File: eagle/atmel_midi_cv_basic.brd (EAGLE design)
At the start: 100 x 80.8 mm, 46 parts, among them IC1 TL072P, IC2 TL072P, U1 ATMEGA328P_PDIP

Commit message: fixed led output to pwm pin and schematic consistent
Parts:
- R25: value 220 -> 470
- moved VEL_LED 39.1 mm to (28.7, 10.2), turned to 270 degrees
- moved R25 22.5 mm to (32.0, 19.1)
- moved C6 17.5 mm to (24.6, 6.35)
- moved R12 14.2 mm to (29.1, 20.6)
- moved C2 13.7 mm to (25.7, 26.4)
- moved R13 13.3 mm to (21.6, 25.4)
- moved C5 12.2 mm to (58.9, 53.3)
- moved CV_BUS_ENABLE 12.2 mm to (69.7, 51.6)
- moved PITCH 12.2 mm to (72.9, 0.00)
- moved R10 12.2 mm to (72.1, 43.2)
- moved R11 12.2 mm to (62.7, 21.6)
- moved R5 12.2 mm to (58.9, 37.8)
- moved R8 12.2 mm to (60.8, 24.8)
- moved SCALE_TRIM 12.2 mm to (62.7, 44.5)
- moved U$4 12.2 mm to (53.8, 25.4)
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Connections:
- new net GND: VEL_LED.K
- net N$18: now also R25.1, VEL_LED.A; no longer R25.2, VEL_LED.K
- net N$20: now also R25.2, U1.12; no longer U1.6, VEL_LED.A
- net N$22: now also U1.6; no longer U1.5
- net N$29: no longer R25.1
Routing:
- net GND: track 0.00 -> 3.72 mm
- net N$28: track 39.6 -> 41.7 mm
- net N$20: track 8.09 -> 6.01 mm
- net +12V: track 144.9 -> 142.9 mm
- net +5V: track 176.7 -> 178.1 mm
- net N$21: track 7.28 -> 8.37 mm
- net N$10: track 13.6 -> 12.9 mm
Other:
- board size 100 x 80.8 mm -> 101 x 80.8 mm

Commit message: cleaned up some routes
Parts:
- R1, R10, R11, R12, R13, R2, R24, R25, R26, R3, R4, R5, R7, R8, R9: device rcl:0207/10 -> rcl:0207/7
- moved R1 3.78 mm to (36.3, 61.0)
- moved R8 3.66 mm to (58.8, 21.7), turned to 90 degrees
- moved RST1 3.21 mm to (29.2, 60.7)
- moved RST2 3.14 mm to (29.2, 64.3)
- moved D1 2.84 mm to (13.2, 52.1)
- moved U$2 2.03 mm to (61.5, 52.1)
- moved VEL_LED 1.83 mm to (29.7, 11.7)
- moved GATE_BUS_ENABLE 1.80 mm to (70.5, 56.3)
- moved R2 1.80 mm to (13.2, 49.5)
- moved CV_BUS_ENABLE 1.78 mm to (67.9, 51.6)
- moved C4 1.48 mm to (53.8, 52.6)
- moved C5 1.37 mm to (57.7, 52.8)
- moved MIDI_IN_4 1.27 mm to (23.4, 50.8)
- moved OK1 1.27 mm to (15.7, 59.7)
- moved SCALE_TRIM 1.27 mm to (62.7, 45.7)
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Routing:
- net N$29: track 346.8 -> 339.8 mm
- net N$32: track 0.00 -> 6.35 mm
- net N$13: track 12.7 -> 7.16 mm
- net +12V: track 142.9 -> 137.6 mm
- net N$9: track 42.8 -> 38.7 mm
- net GND: track 3.72 -> 0.00 mm
- net N$17: track 57.9 -> 54.3 mm
- net N$43: track 7.40 -> 10.7 mm
- net N$30: track 37.7 -> 34.5 mm
- net N$28: track 41.7 -> 44.2 mm
- net N$8: track 4.02 -> 6.48 mm
- net N$27: track 5.80 -> 7.46 mm
- net N$14: track 11.1 -> 9.57 mm
- net N$3: track 10.3 -> 11.7 mm
- net N$7: track 8.90 -> 10.3 mm
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
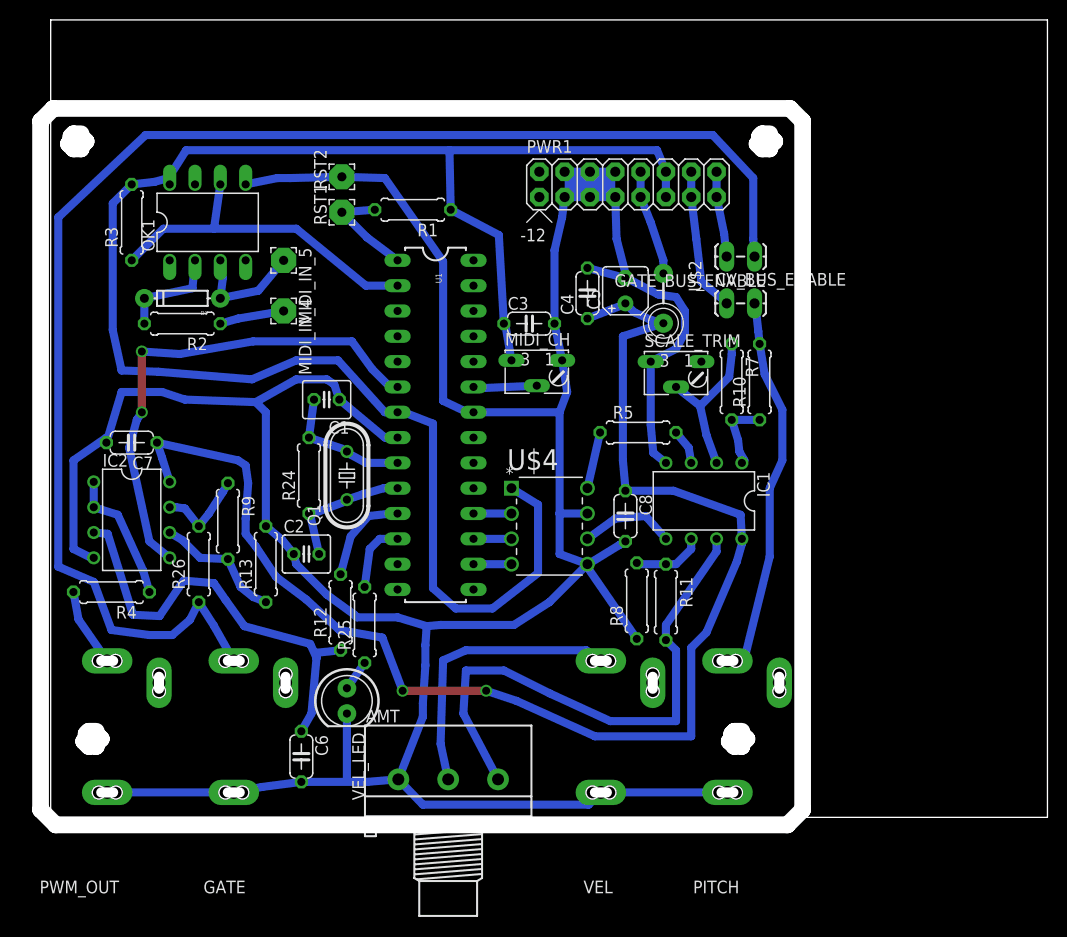
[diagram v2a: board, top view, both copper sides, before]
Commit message: corrected wrong gate pin and tl072 back to bipolar to prevent locking
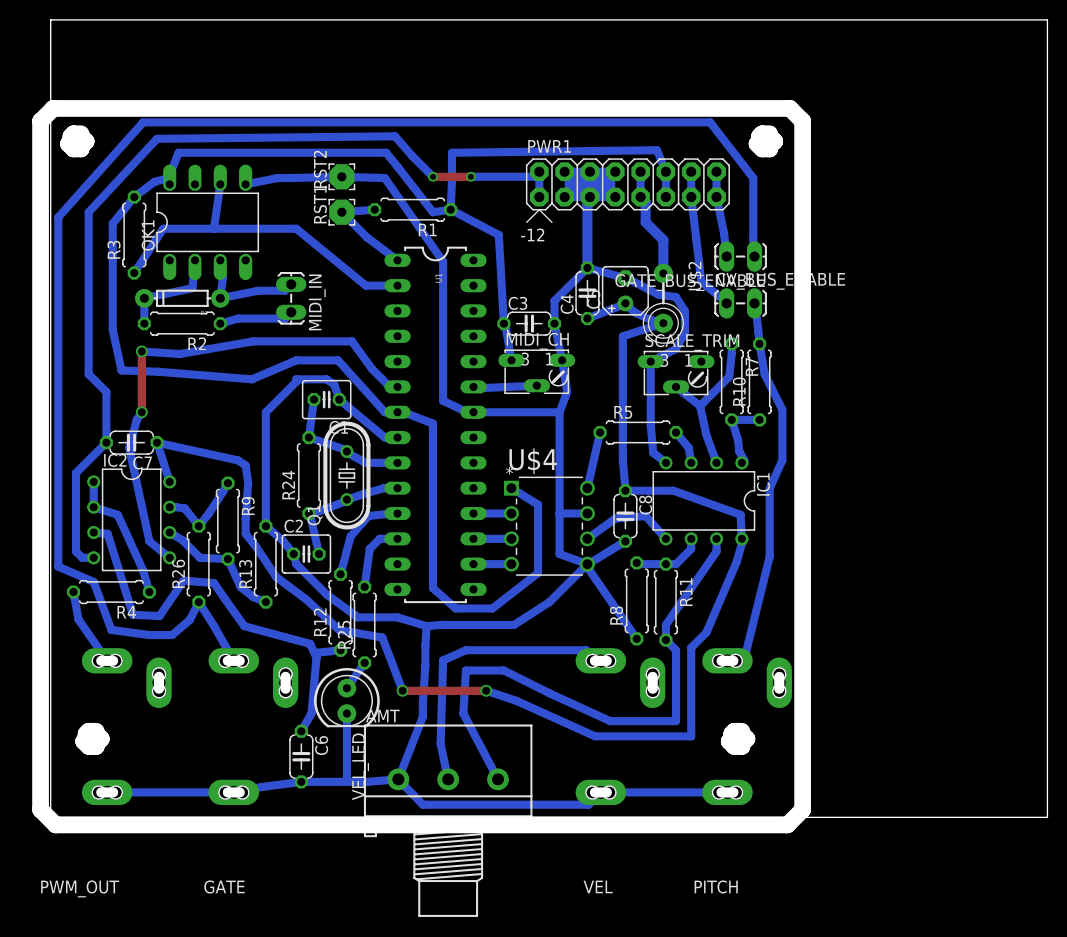
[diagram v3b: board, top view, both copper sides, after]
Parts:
- removed MIDI_IN_4: midi pin 4, wirepad:2,54/0,9
- removed MIDI_IN_5: midi pin 5, wirepad:2,54/0,9
- added MIDI_IN: M02LOCK_LONGPADS, SparkFun-Connectors:1X02_LOCK_LONGPADS
- moved R3 1.30 mm to (8.38, 58.4)
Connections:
- new net -12V: C7.2, IC2.4, PWR1.1, PWR1.2
- net N$29: no longer C7.2, IC2.4
- net N$3: now also MIDI_IN.1; no longer MIDI_IN_5.1
- net N$8: now also MIDI_IN.2; no longer MIDI_IN_4.1
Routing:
- net -12V: track 0.00 -> 91.0 mm, vias 0 -> 2
- net N$29: track 339.8 -> 296.5 mm
- net N$31: track 144.1 -> 146.0 mm
- net +5V: track 176.8 -> 178.5 mm
- net N$8: track 6.48 -> 7.45 mm
- net N$30: track 34.5 -> 35.3 mm
- net N$11: track 10.6 -> 11.1 mm

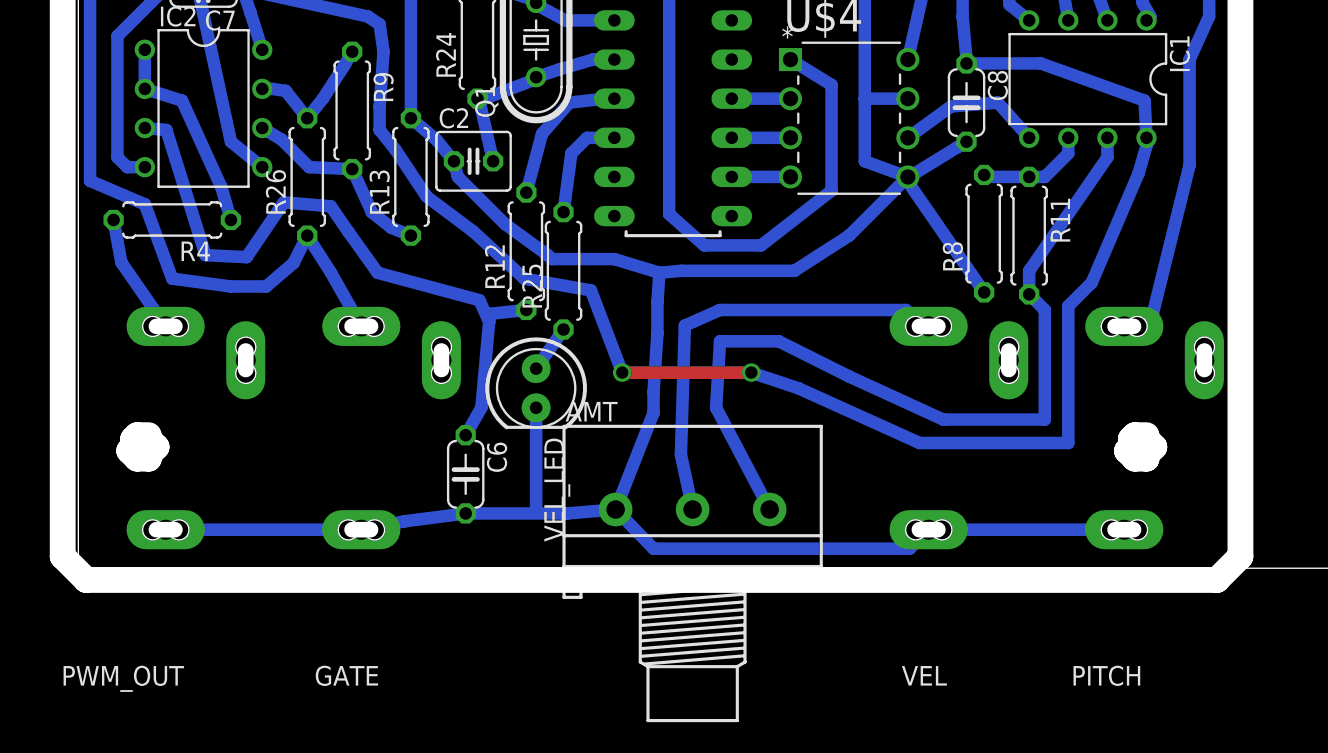
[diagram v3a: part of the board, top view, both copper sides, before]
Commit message: rail2rail pitch amp, tone output, improved decoupling, board mount midi jack, more isolation
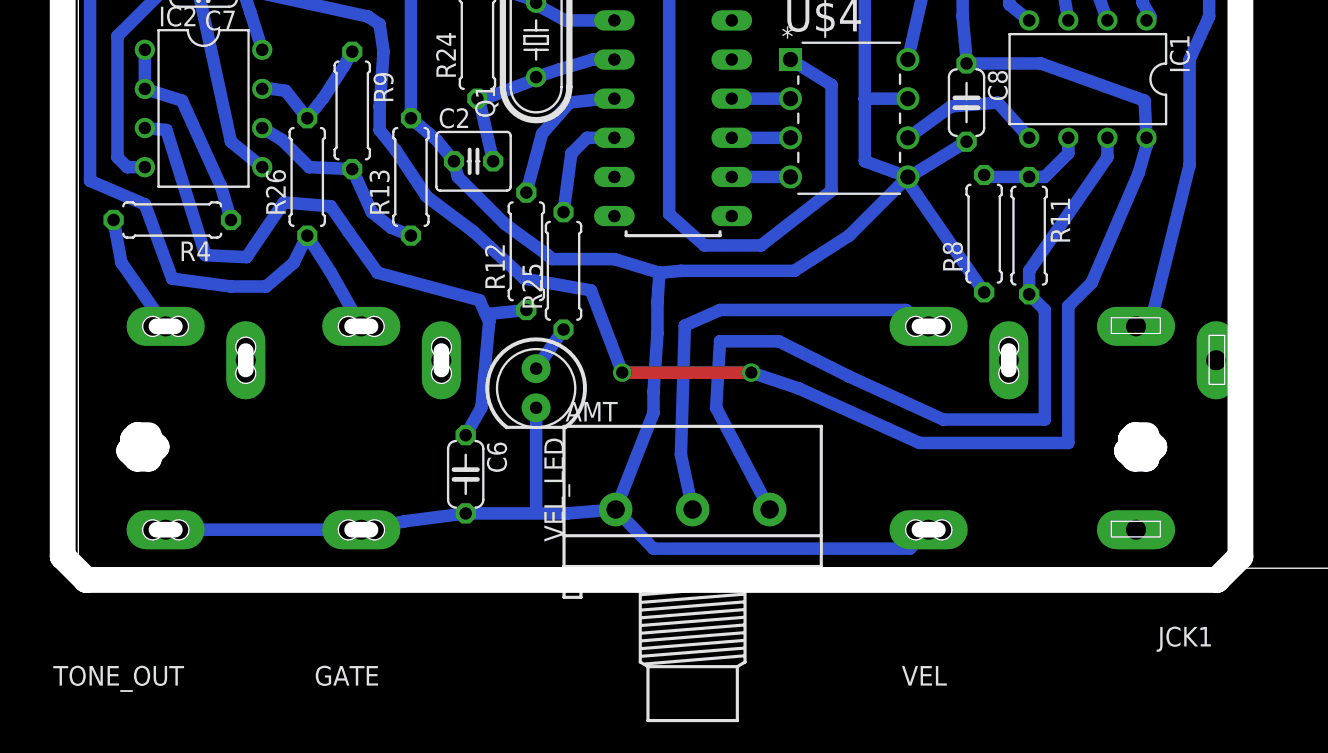
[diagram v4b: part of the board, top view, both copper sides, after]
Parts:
- removed PITCH: AUDIO-JACK, erthenvar:ERTHENVAR-JACK-90DEG
- added JCK1: AUDIO-JACKITEAD, erthenvar:JACK-90DEG-ITEAD
- renumbered PWM_OUT to TONE_OUT
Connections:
- net N$21: now also U1.19; no longer U1.11
- net N$29: now also JCK1.P$1; no longer PITCH.P$1
- net N$9: now also JCK1.P$3; no longer PITCH.P$3
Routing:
- net N$29: track 296.5 -> 283.8 mm
- net N$9: track 38.7 -> 37.1 mm
- net N$21: track 9.58 -> 8.94 mm
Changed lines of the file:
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@@
 <?xml version="1.0" encoding="utf-8"?>
 <!DOCTYPE eagle SYSTEM "eagle.dtd">
-<eagle version="7.1.0">
+<eagle version="7.6.0">
 <drawing>
 <settings>
@@
 <attribute name="OC_FARNELL" value="9860150" x="15.748" y="59.69" size="1.778" layer="27" display="off"/>
 </element>
-<element name="PITCH" library="erthenvar" package="ERTHENVAR-JACK-90DEG" value="AUDIO-JACK" x="72.898" y="0" rot="R180"/>
-<element name="PWM_OUT" library="erthenvar" package="ERTHENVAR-JACK-90DEG" value="AUDIO-JACK" x="10.668" y="0" rot="R180"/>
+<element name="TONE_OUT" library="erthenvar" package="ERTHENVAR-JACK-90DEG" value="AUDIO-JACK" x="10.668" y="0" rot="R180"/>
 <element name="PWR1" library="eurorack" package="POWER_16" value="POWER" x="55.372" y="63.5"/>
 <element name="Q1" library="crystal" package="HC49/S" value="" x="29.718" y="34.29" rot="R90">
@@
 <element name="CV_BUS_ENABLE" library="SparkFun-Connectors" package="1X02_LOCK_LONGPADS" value="M02LOCK_LONGPADS" x="67.945" y="51.562"/>
 <element name="MIDI_IN" library="SparkFun-Connectors" package="1X02_LOCK_LONGPADS" value="M02LOCK_LONGPADS" x="24.13" y="53.34" rot="R270"/>
+<element name="JCK1" library="erthenvar" package="JACK-90DEG-ITEAD" value="AUDIO-JACKITEAD" x="73.66" y="0" rot="R180"/>
 </elements>
 <signals>
@@
 </signal>
 <signal name="N$9">
-<contactref element="PITCH" pad="P$3"/>
 <contactref element="R10" pad="2"/>
 <contactref element="CV_BUS_ENABLE" pad="2"/>
@@
 <wire x1="70.993" y1="48.768" x2="71.12" y2="47.498" width="0.8128" layer="16"/>
 <wire x1="70.485" y1="51.308" x2="70.612" y2="51.562" width="0.8128" layer="16"/>
-<wire x1="67.898" y1="15.7" x2="69.548" y2="15.7" width="0.8128" layer="16"/>
 <wire x1="69.548" y1="15.7" x2="72.136" y2="26.162" width="0.8128" layer="16"/>
 <wire x1="72.136" y1="26.162" x2="72.136" y2="33.02" width="0.8128" layer="16"/>
@@
 <wire x1="73.406" y1="40.894" x2="71.628" y2="44.45" width="0.8128" layer="16"/>
 <wire x1="71.628" y1="44.45" x2="71.12" y2="47.498" width="0.8128" layer="16"/>
+<contactref element="JCK1" pad="P$3"/>
+<wire x1="68.66" y1="15.7" x2="69.548" y2="15.7" width="0" layer="19" extent="16-16"/>
 </signal>
 <signal name="N$12">
@@
 </signal>
 <signal name="N$21">
-<contactref element="U1" pad="11"/>
 <contactref element="R12" pad="2"/>
 <wire x1="31.877" y1="30.226" x2="30.099" y2="28.194" width="0.8128" layer="16"/>
 <wire x1="34.163" y1="30.48" x2="31.877" y2="30.226" width="0.8128" layer="16"/>
-<wire x1="34.798" y1="30.48" x2="34.163" y2="30.48" width="0.8128" layer="16"/>
 <wire x1="30.099" y1="28.194" x2="29.083" y2="24.384" width="0.8128" layer="16"/>
+<contactref element="U1" pad="19"/>
+<wire x1="34.163" y1="30.48" x2="42.418" y2="33.02" width="0" layer="19" extent="16-16"/>
 </signal>
 <signal name="N$23">
@@
 <signal name="N$24">
 <contactref element="R4" pad="2"/>
-<contactref element="PWM_OUT" pad="P$3"/>
+<contactref element="TONE_OUT" pad="P$3"/>
 <wire x1="2.286" y1="22.606" x2="2.794" y2="19.844" width="0.8128" layer="16"/>
 <wire x1="2.794" y1="19.844" x2="5.668" y2="15.7" width="0.8128" layer="16"/>
@@
 <contactref element="C4" pad="2"/>
 <contactref element="VEL" pad="P$1"/>
-<contactref element="PITCH" pad="P$1"/>
 <contactref element="SCALE_TRIM" pad="E"/>
-<contactref element="PWM_OUT" pad="P$1"/>
+<contactref element="TONE_OUT" pad="P$1"/>
 <contactref element="C6" pad="2"/>
 <contactref element="IC1" pad="4"/>
@@
 <wire x1="37.338" y1="1.27" x2="53.968" y2="1.27" width="0.8128" layer="16"/>
 <wire x1="53.968" y1="1.27" x2="55.198" y2="2.5" width="0.8128" layer="16"/>
-<wire x1="55.198" y1="2.5" x2="67.898" y2="2.5" width="0.8128" layer="16"/>
 <wire x1="53.848" y1="30.48" x2="51.054" y2="30.48" width="0.8128" layer="16"/>
 <wire x1="50.546" y1="49.53" x2="51.308" y2="45.847" width="0.8128" layer="16"/>
@@
 <wire x1="53.848" y1="55.118" x2="53.848" y2="61.468" width="1.016" layer="16"/>
 <wire x1="53.848" y1="61.468" x2="54.61" y2="62.23" width="1.016" layer="16"/>
+<contactref element="JCK1" pad="P$1"/>
+<wire x1="68.66" y1="2.5" x2="5.668" y2="2.5" width="0" layer="19" extent="1-1"/>
 </signal>
 <signal name="N$18">
